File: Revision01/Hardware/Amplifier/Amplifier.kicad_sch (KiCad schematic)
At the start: 13 parts, among them U1 INA333AIDGKR, U2 TLV9061SQDBVRQ1

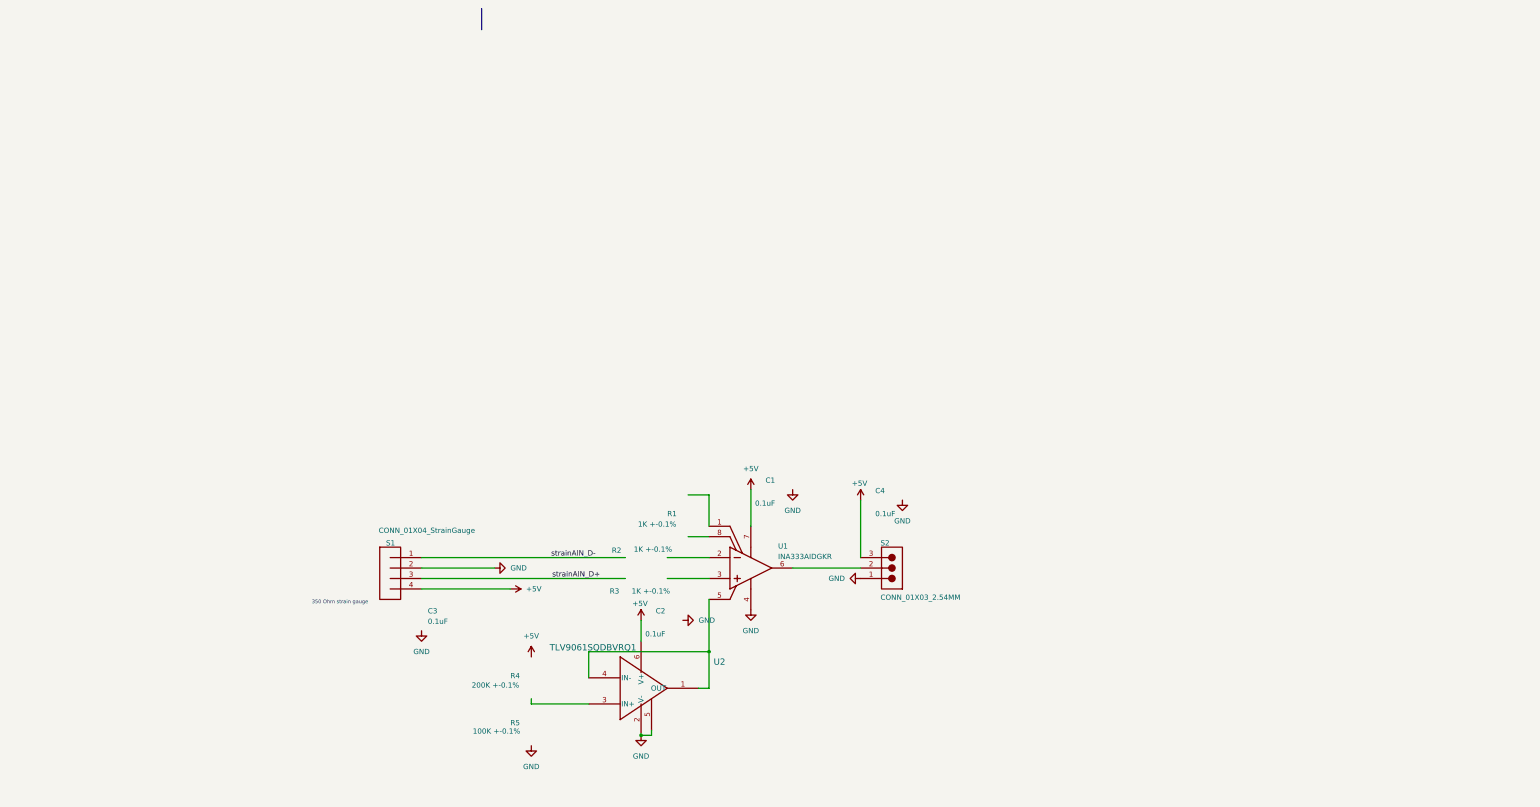
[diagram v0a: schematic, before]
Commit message: . Moved R from main board to amplifier board to current limit the INA amplifier in case of cable short to GND . replaced RC filter with 500ohm, 6.8nF, in order to current limit the INA amplifier to 10mA, keeping a ~40-50kHz 3db frequency. . Reworked Hub layout. . Reworked Hub component columns for Digikey, Mouser, & Aliexpress.
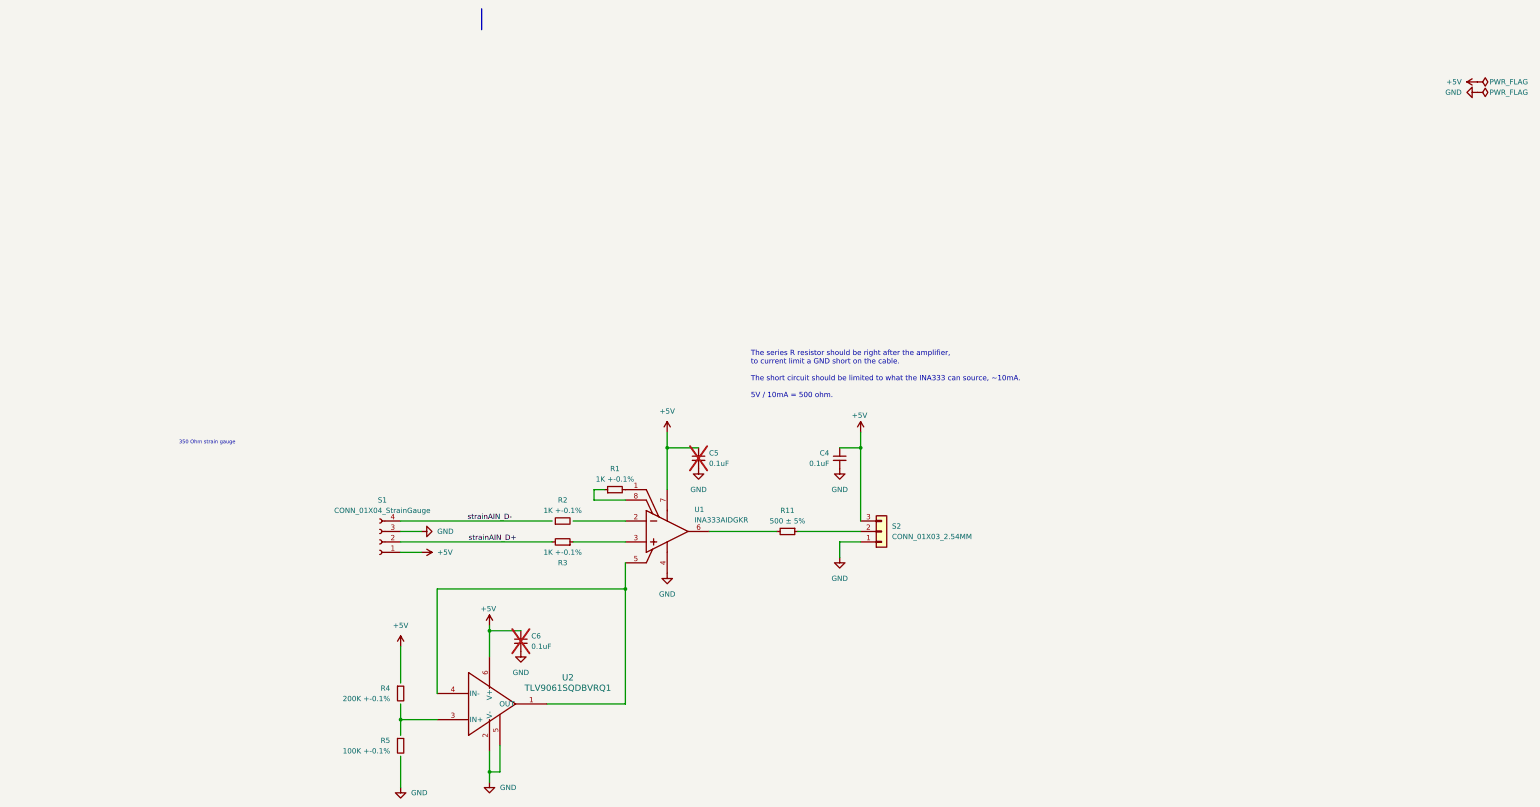
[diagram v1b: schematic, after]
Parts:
- removed C1, C2: 0.1uF, Capacitor_SMD:C_0805_2012Metric_Pad1.18x1.45mm_HandSolder, symbol StrainAmplifierV1:root_0_CAP_0805_GenericSchematic-library.SchLib
- removed C3: 0.1uF, Capacitor_SMD:C_0805_2012Metric_Pad1.18x1.45mm_HandSolder, symbol StrainAmplifierV1:root_1_CAP_0805_GenericSchematic-library.SchLib
- added C5, C6: 0.1uF, Capacitor_SMD:C_0805_2012Metric_Pad1.18x1.45mm_HandSolder, symbol Device:C_Small
- added R11: 500 ± 5%, Resistor_SMD:R_0805_2012Metric_Pad1.20x1.40mm_HandSolder, symbol Device:R_Small
- C4: symbol StrainAmplifierV1:root_2_CAP_0805_GenericSchematic-library.SchLib -> Device:C_Small; DISTRIBUTOR LINK https://www.digikey.ca/en/products/detail/yageo/CC0805JRNPO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 -> (none); MANUFACTURER YAGEO -> (none); MANUFACTURER PART NUMBER CC0805JRNPO9BN250 -> (none); VOLTAGE RATING 50 -> (none)
- R1: symbol StrainAmplifierV1:root_1_RES_0805_GenericSchematic-library.SchLib -> Device:R_Small; DISTRIBUTOR LINK https://www.digikey.ca/en/products/detail/stackpole-electro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 -> (none); MANUFACTURER Stackpole Electronics Inc -> (none); MANUFACTURER PART NUMBER RNCS0805BKE1K00 -> (none)
- R2, R3: symbol StrainAmplifierV1:root_2_RES_0805_GenericSchematic-library.SchLib -> Device:R_Small; DISTRIBUTOR LINK https://www.digikey.ca/en/products/detail/stackpole-electro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 -> (none); MANUFACTURER Stackpole Electronics Inc -> (none); MANUFACTURER PART NUMBER RNCS0805BKE1K00 -> (none)
- R4: symbol StrainAmplifierV1:root_1_RES_0805_GenericSchematic-library.SchLib -> Device:R_Small; DISTRIBUTOR LINK https://www.digikey.ca/en/products/detail/koa-speer-electro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 -> (none); MANUFACTURER KOA Speer Electronics, Inc. -> (none); MANUFACTURER PART NUMBER RN73R2ATTD2003B25 -> (none)
- R5: symbol StrainAmplifierV1:root_1_RES_0805_GenericSchematic-library.SchLib -> Device:R_Small; DISTRIBUTOR LINK https://www.digikey.ca/en/products/detail/stackpole-electro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 -> (none); MANUFACTURER Stackpole Electronics Inc -> (none); MANUFACTURER PART NUMBER RNCS0805BKE100K -> (none)
- S1: footprint StrainAmplifierV1:CONN_01X04 -> Amplifier:CONN_01X04; symbol StrainAmplifierV1:root_0_CONN_01X04_StrainGauge_GenericSchematic-library.SchLib -> Connector:Conn_01x04_Socket
- S2: symbol StrainAmplifierV1:root_2_mirrored_CONN_01X03_2.54MM_GenericSchematic-library.SchLib -> Connector_Generic:Conn_01x03
- U1: footprint Package_SO:VSSOP-8_3x3mm_P0.65mm -> Amplifier:INA333AIDGKR_SOP65P490X110-8N; symbol StrainAmplifierV1:root_0_TI-INAXXXXXX8_Altium Content Vault -> Amplifier:root_0_TI-INAXXXXXX8_Altium Content Vault; CMRR(MIN)(DB) 100 -> (none); CODE_JEDEC MO-187 -> (none); COMPONENTLINK1DESCRIPTION Manufacturer URL -> (none); COMPONENTLINK1URL http://www.ti.com/ -> (none); COMPONENTLINK2DESCRIPTION Datasheet -> (none); COMPONENTLINK2URL http://www.ti.com/general/docs/lit/getliterature.tsp?generi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 -> (none); COMPONENTLINK3DESCRIPTION Package Specification -> (none); COMPONENTLINK3URL http://www.ti.com/litv/pdf/mpds028d -> (none); DATASHEETVERSION SBOS445B -> (none); ECO-PLAN Green (RoHS & no Sb/Br) -> (none); GAIN(V/V) 1 to 1000 -> (none); INPUT BIAS CURRENT (+/-)(MAX)(NA) 0.2 -> (none); INPUT OFFSET (+/-)(MAX)(UV) 25 -> (none); INPUT OFFSET DRIFT (+/-)(MAX)(UV/DEGREES CELSIUS) 0.1 -> (none); MANUFACTURER Texas Instruments -> (none); MOUNTING TECHNOLOGY Surface Mount -> (none); NOISE AT 1KHZ(TYP)(NV/RT(HZ)) 50 -> (none); NUMBER OF CHANNELS 1 -> (none); OUTPUT OFFSET (+/-)(MAX)(UV) 75/G -> (none); OUTPUT OFFSET DRIFT (+/-)(MAX)(UV/DEGREES CELSIUS) 0.5/G -> (none); PACKAGEDESCRIPTION 8-Pin Thin Small Outline, Body 3 x 3 mm, Pitch 0.65 mm -> (none); PACKAGEREFERENCE DGK0008A -> (none); PACKAGEVERSION 4073329/E, 05/2006 -> (none); PARTNUMBER INA333AIDGKR -> (none); QUIESCENT CURRENT (+/-)(TYP)(MA) 0.05 -> (none); SUBFAMILY Single Supply -> (none); VS(MAX)(V) 5.5 -> (none); VS(MIN)(V) 1.8 -> (none)
- U2: symbol StrainAmplifierV1:TLV9061SQDBVRQ1 -> Amplifier:TLV9061SQDBVRQ1
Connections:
- net +5V: now also C4.1, S1.1 (Pin_1), C5.1, C6.1; no longer S1.4
- net GND: now also C4.2, S1.3 (Pin_3), C5.2, C6.2; no longer S1.2
- net strainAIN_D+: now also R3.2, S1.2 (Pin_2); no longer S1.3
- net strainAIN_D-: now also S1.4 (Pin_4); no longer S1.1
- net at S2.2 (Pin_2): now also R11.1; no longer U1.6 (VOUT)
- net at U1.1 (RG): now also R1.2
- net at U1.3 (VIN+): now also R3.1
- net at U1.8 (RG): now also R1.1
- new net: R11.2, U1.6 (VOUT)
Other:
- note added: "The series R resistor should be right after the amplifier, to current limit a GND short on the cable. The short circuit should be limited to what the INA333 can source, ~10mA. 5V / 10mA = 500 ohm."
- moved on the sheet: U1, U2

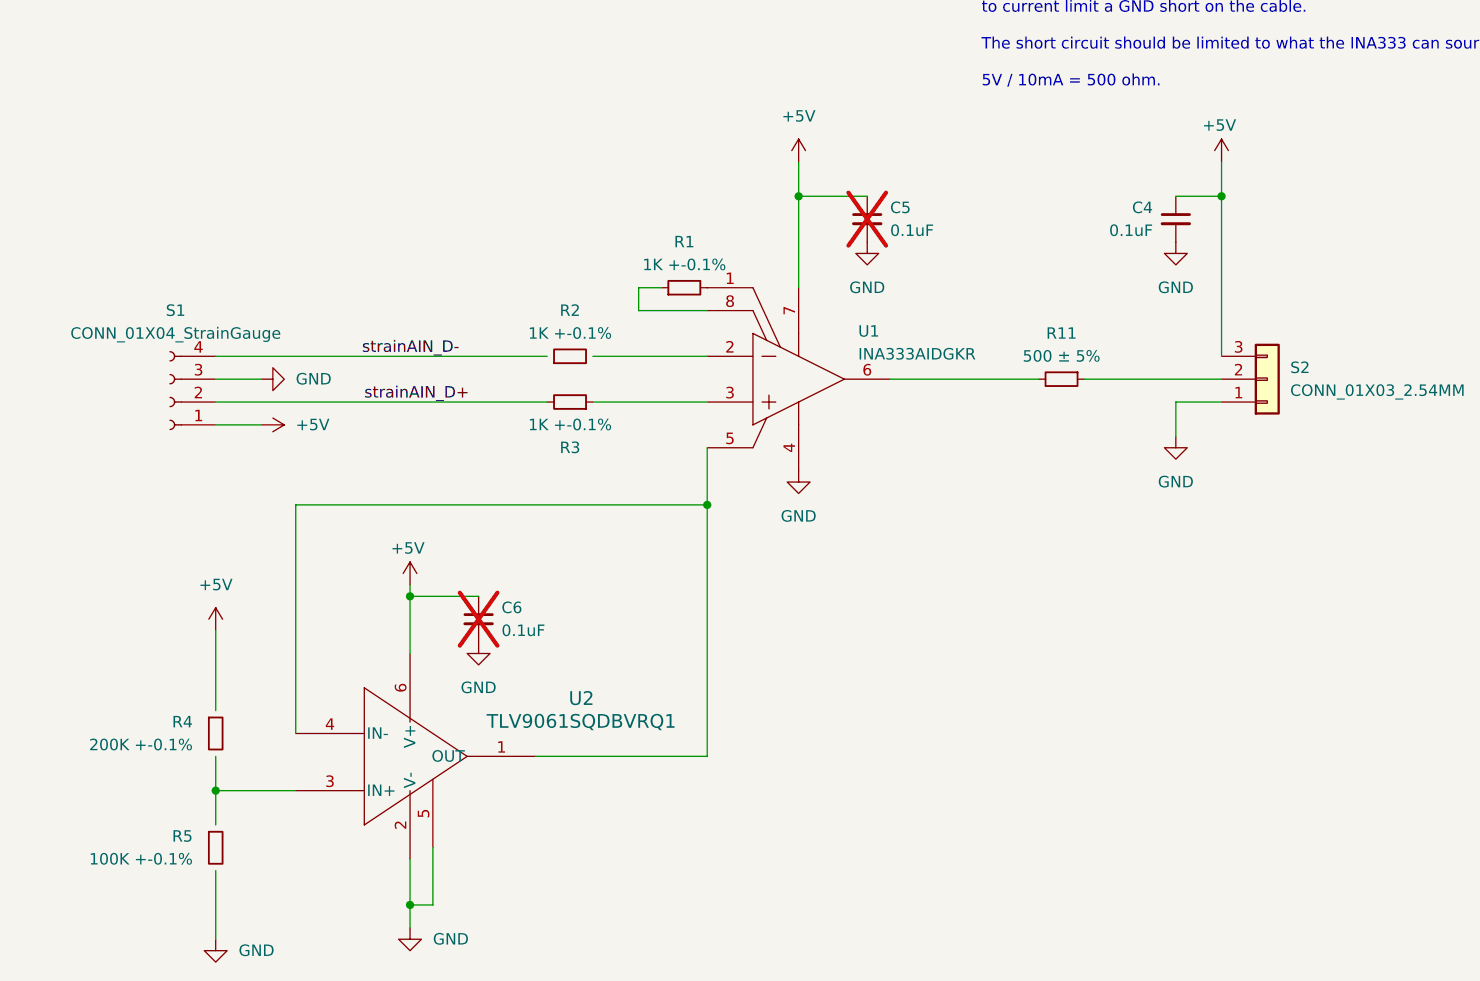
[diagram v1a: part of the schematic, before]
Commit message: . Amplifier layout WIP draft with 500 ohm resistor . Hub layout final draft, added 100 ohm series resistor to AIN
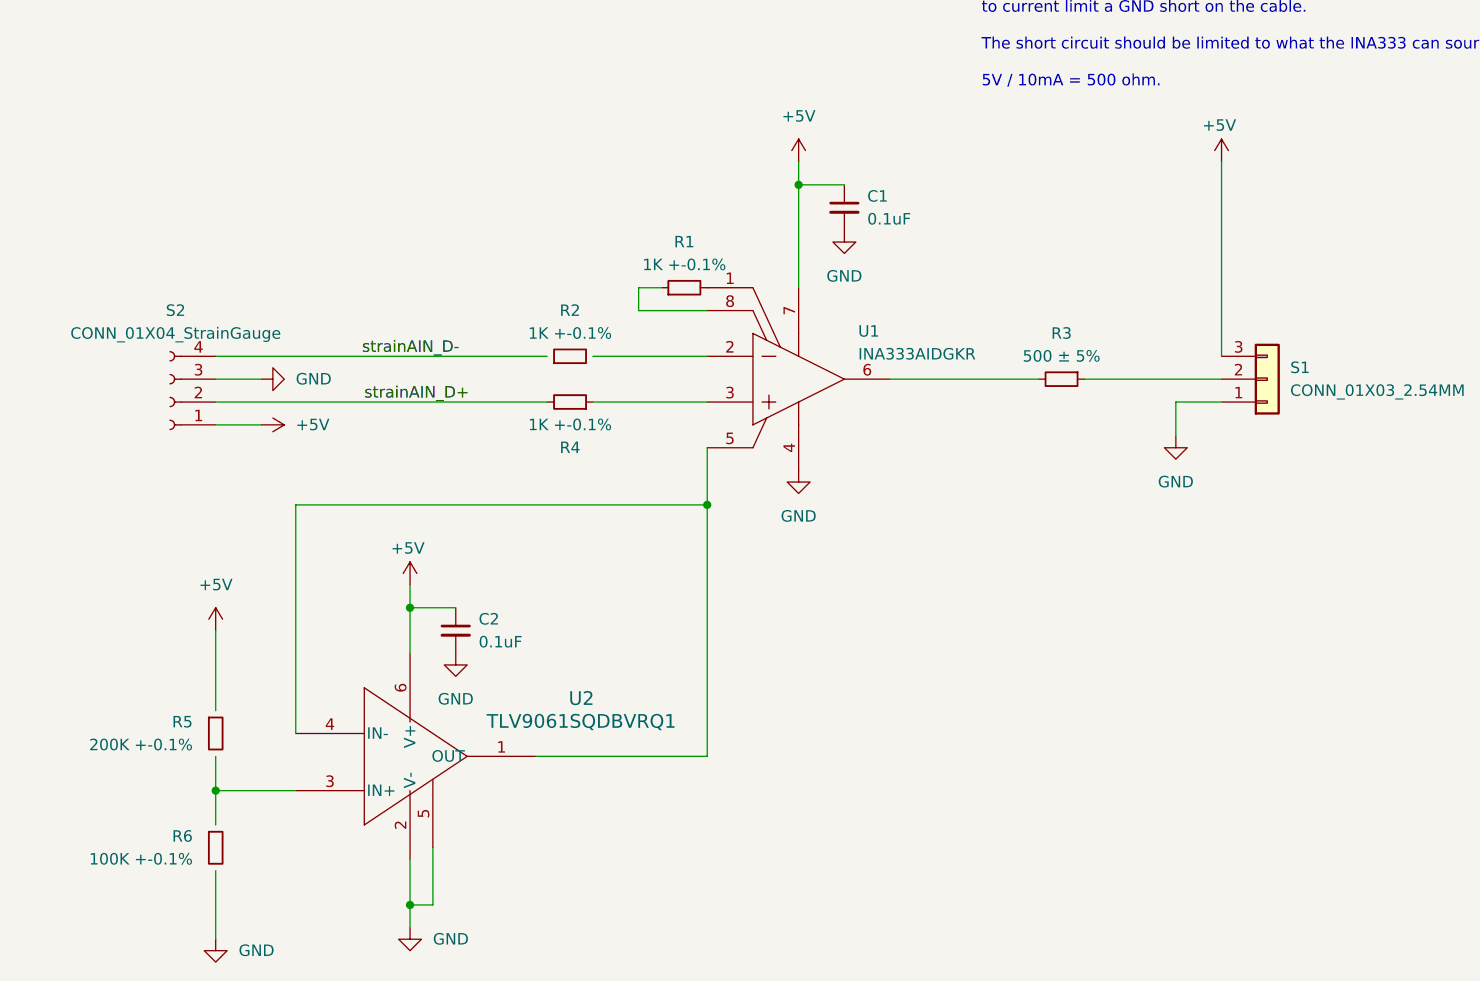
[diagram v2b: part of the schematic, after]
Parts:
- removed C5, C6: 0.1uF, Capacitor_SMD:C_0805_2012Metric_Pad1.18x1.45mm_HandSolder, symbol Device:C_Small
- added C2: 0.1uF, Capacitor_SMD:C_0805_2012Metric_Pad1.18x1.45mm_HandSolder, symbol Device:C_Small
- renumbered C4 to C1, R11 to R3, R3 to R4, R4 to R5, R5 to R6, S2 to S1, S1 to S2
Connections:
- net +5V: now also C2.1
- net GND: now also C2.2
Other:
- moved on the sheet: C1
